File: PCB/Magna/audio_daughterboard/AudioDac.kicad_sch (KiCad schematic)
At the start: 66 parts, among them U401 PCM1789, U402 NE5532, U403 NE5532

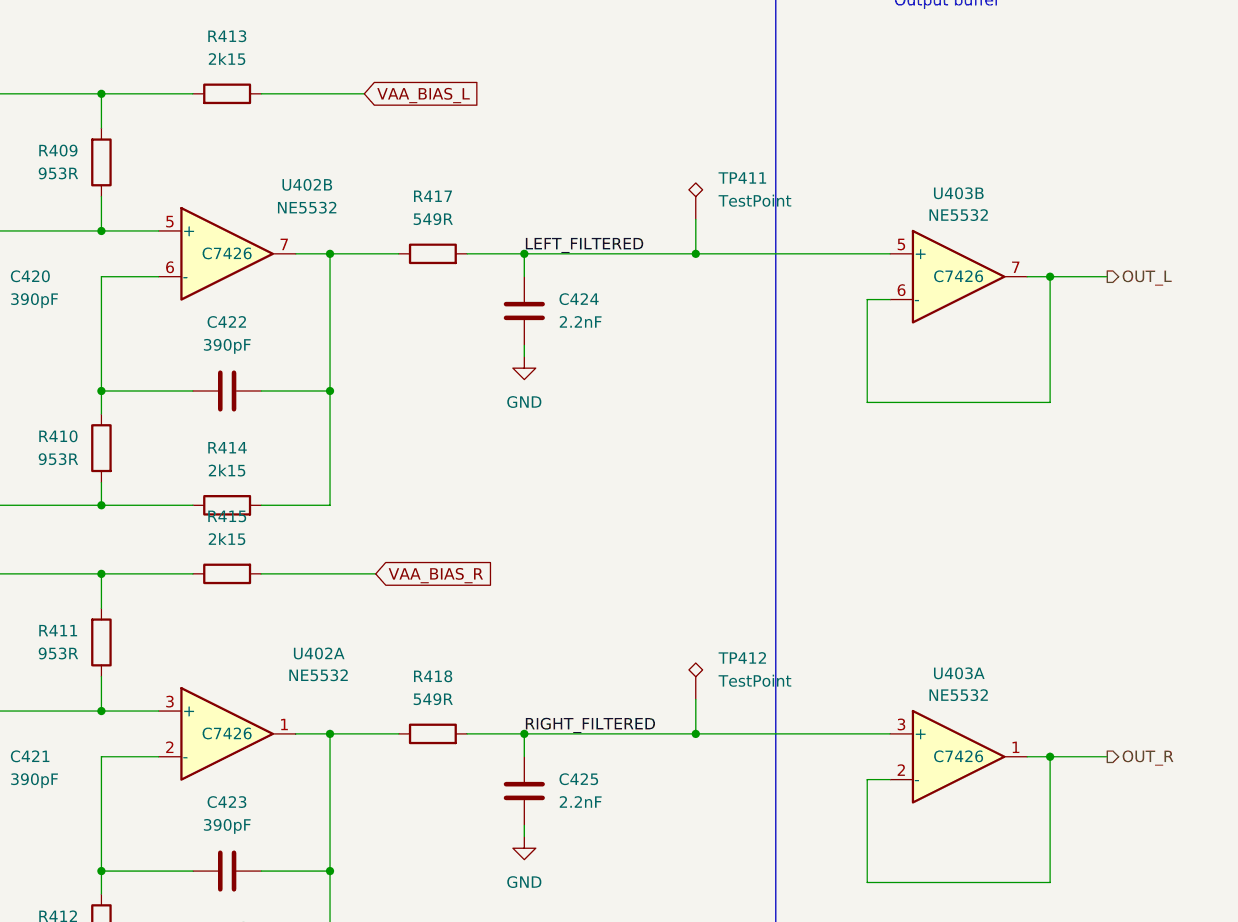
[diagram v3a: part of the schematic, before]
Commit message: Start layout and routing of Audio Daugherboard
Also a lot of small changes to everything that became apperant
when the audio daughterboard was designed. Such as the Headphone
PCB, which is now separate from the rest of the audio.
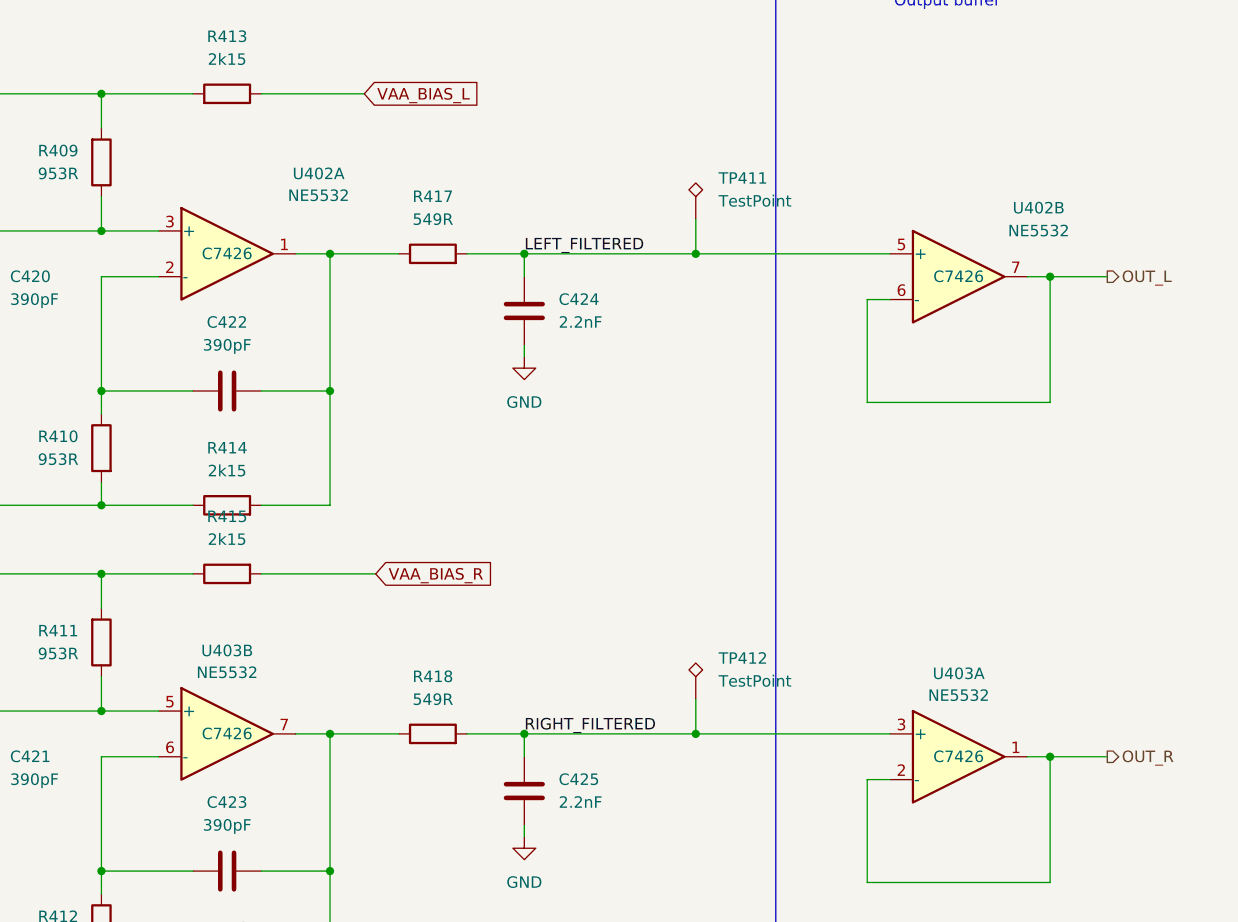
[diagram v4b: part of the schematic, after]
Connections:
- net LEFT_FILTERED: now also U402.5 (+); no longer U403.5 (+)
- net OUT_L: now also U402.6 (-), U402.7; no longer U403.6 (-), U403.7
- net at C423.1, R412.1: now also U403.6 (-); no longer U402.2 (-)
- net at C423.2, R416.2, R418.1: now also U403.7; no longer U402.1
- net at C421.1, R411.1: now also U403.5 (+); no longer U402.3 (+)
- net at C420.1, R409.1: now also U402.3 (+); no longer U402.5 (+)
- net at C422.2, R414.2, R417.1: now also U402.1; no longer U402.7
- net at C422.1, R410.1: now also U402.2 (-); no longer U402.6 (-)
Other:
- moved on the sheet: U402A, U402B, U403B
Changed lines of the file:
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@@
 	(symbol
 		(lib_id "Amplifier_Operational:NE5532")
-		(at 289.56 100.33 0)
+		(at 289.56 46.99 0)
 		(unit 1)
 		(exclude_from_sim no)
@@
 		(dnp no)
 		(property "Reference" "U402"
-			(at 299.72 91.44 0)
+			(at 299.72 38.1 0)
 			(effects
 				(font
@@
 		)
 		(property "Value" "NE5532"
-			(at 299.72 93.8643 0)
+			(at 299.72 40.5243 0)
 			(effects
 				(font
@@
 		)
 		(property "Footprint" "Package_SO:SOIC-8_3.9x4.9mm_P1.27mm"
-			(at 289.56 100.33 0)
+			(at 289.56 46.99 0)
 			(effects
 				(font
@@
 		)
 		(property "Datasheet" "http://www.ti.com/lit/ds/symlink/ne5532.pdf"
-			(at 289.56 100.33 0)
+			(at 289.56 46.99 0)
 			(effects
 				(font
@@
 		)
 		(property "Description" "Dual Low-Noise Operational Amplifiers, DIP-8/SOIC-8"
-			(at 289.56 100.33 0)
+			(at 289.56 46.99 0)
 			(effects
 				(font
@@
 		)
 		(property "Sim.Device" "SUBCKT"
-			(at 289.56 100.33 0)
+			(at 289.56 46.99 0)
 			(effects
 				(font
@@
 		)
 		(property "Sim.Library" "${KICAD7_SYMBOL_DIR}/Simulation_SPICE.sp"
-			(at 289.56 100.33 0)
+			(at 289.56 46.99 0)
 			(effects
 				(font
@@
 		)
 		(property "Sim.Name" "kicad_builtin_opamp_dual"
-			(at 289.56 100.33 0)
+			(at 289.56 46.99 0)
 			(effects
 				(font
@@
 		)
 		(property "Sim.Pins" "1=out1 2=in1- 3=in1+ 4=vee 5=in2+ 6=in2- 7=out2 8=vcc"
-			(at 289.56 100.33 0)
+			(at 289.56 46.99 0)
 			(effects
 				(font
@@
 		)
 		(property "Sim.Params" "GAIN=10M ROUT=0.3"
-			(at 289.56 100.33 0)
+			(at 289.56 46.99 0)
 			(effects
 				(font
@@
 		)
 		(property "LCSC" "C7426"
-			(at 289.56 100.33 0)
+			(at 289.56 46.99 0)
 			(effects
 				(font
@@
 		)
 		(property "Field5" ""
-			(at 289.56 100.33 0)
+			(at 289.56 46.99 0)
 			(effects
 				(font
@@
 	(symbol
 		(lib_id "Amplifier_Operational:NE5532")
-		(at 289.56 46.99 0)
+		(at 370.84 49.53 0)
 		(unit 2)
 		(exclude_from_sim no)
@@
 		(fields_autoplaced yes)
 		(property "Reference" "U402"
-			(at 298.45 39.37 0)
+			(at 379.73 41.91 0)
 			(effects
 				(font
@@
 		)
 		(property "Value" "NE5532"
-			(at 298.45 41.91 0)
+			(at 379.73 44.45 0)
 			(effects
 				(font
@@
 		)
 		(property "Footprint" "Package_SO:SOIC-8_3.9x4.9mm_P1.27mm"
-			(at 289.56 46.99 0)
+			(at 370.84 49.53 0)
 			(effects
 				(font
@@
 		)
 		(property "Datasheet" "http://www.ti.com/lit/ds/symlink/ne5532.pdf"
-			(at 289.56 46.99 0)
+			(at 370.84 49.53 0)
 			(effects
 				(font
@@
 		)
 		(property "Description" "Dual Low-Noise Operational Amplifiers, DIP-8/SOIC-8"
-			(at 289.56 46.99 0)
+			(at 370.84 49.53 0)
 			(effects
 				(font
@@
 		)
 		(property "Sim.Device" "SUBCKT"
-			(at 289.56 46.99 0)
+			(at 370.84 49.53 0)
 			(effects
 				(font
@@
 		)
 		(property "Sim.Library" "${KICAD7_SYMBOL_DIR}/Simulation_SPICE.sp"
-			(at 289.56 46.99 0)
+			(at 370.84 49.53 0)
 			(effects
 				(font
@@
 		)
 		(property "Sim.Name" "kicad_builtin_opamp_dual"
-			(at 289.56 46.99 0)
+			(at 370.84 49.53 0)
 			(effects
 				(font
@@
 		)
 		(property "Sim.Pins" "1=out1 2=in1- 3=in1+ 4=vee 5=in2+ 6=in2- 7=out2 8=vcc"
-			(at 289.56 46.99 0)
+			(at 370.84 49.53 0)
 			(effects
 				(font
@@
 		)
 		(property "Sim.Params" "GAIN=10M ROUT=0.3"
-			(at 289.56 46.99 0)
+			(at 370.84 49.53 0)
 			(effects
 				(font
@@
 		)
 		(property "LCSC" "C7426"
-			(at 289.56 46.99 0)
+			(at 370.84 49.53 0)
 			(effects
 				(font
@@
 		)
 		(property "Field5" ""
-			(at 289.56 46.99 0)
+			(at 370.84 49.53 0)
 			(effects
 				(font
@@
 	(symbol
 		(lib_id "Amplifier_Operational:NE5532")
-		(at 370.84 49.53 0)
+		(at 289.56 100.33 0)
 		(unit 2)
 		(exclude_from_sim no)
@@
 		(fields_autoplaced yes)
 		(property "Reference" "U403"
-			(at 370.84 40.3055 0)
+			(at 289.56 91.1055 0)
 			(effects
 				(font
@@
 		)
 		(property "Value" "NE5532"
-			(at 370.84 42.7298 0)
+			(at 289.56 93.5298 0)
 			(effects
 				(font
@@
 		)
 		(property "Footprint" "Package_SO:SOIC-8_3.9x4.9mm_P1.27mm"
-			(at 370.84 49.53 0)
+			(at 289.56 100.33 0)
 			(effects
 				(font
@@
 		)
 		(property "Datasheet" "http://www.ti.com/lit/ds/symlink/ne5532.pdf"
-			(at 370.84 49.53 0)
+			(at 289.56 100.33 0)
 			(effects
 				(font
@@
 		)
 		(property "Description" "Dual Low-Noise Operational Amplifiers, DIP-8/SOIC-8"
-			(at 370.84 49.53 0)
+			(at 289.56 100.33 0)
 			(effects
 				(font
@@
 		)
 		(property "Sim.Device" "SUBCKT"
-			(at 370.84 49.53 0)
+			(at 289.56 100.33 0)
 			(effects
 				(font
@@
 		)
 		(property "Sim.Library" "${KICAD7_SYMBOL_DIR}/Simulation_SPICE.sp"
-			(at 370.84 49.53 0)
+			(at 289.56 100.33 0)
 			(effects
 				(font
@@
 		)
 		(property "Sim.Name" "kicad_builtin_opamp_dual"
-			(at 370.84 49.53 0)
+			(at 289.56 100.33 0)
 			(effects
 				(font
@@
 		)
 		(property "Sim.Pins" "1=out1 2=in1- 3=in1+ 4=vee 5=in2+ 6=in2- 7=out2 8=vcc"
-			(at 370.84 49.53 0)
+			(at 289.56 100.33 0)
 			(effects
 				(font
@@
 		)
 		(property "Sim.Params" "GAIN=10M"
-			(at 370.84 49.53 0)
+			(at 289.56 100.33 0)
 			(effects
 				(font
@@
 		)
 		(property "LCSC" "C7426"
-			(at 370.84 49.53 0)
+			(at 289.56 100.33 0)
 			(effects
 				(font
@@
 		)
 		(property "Field5" ""
-			(at 370.84 49.53 0)
+			(at 289.56 100.33 0)
 			(effects
 				(font

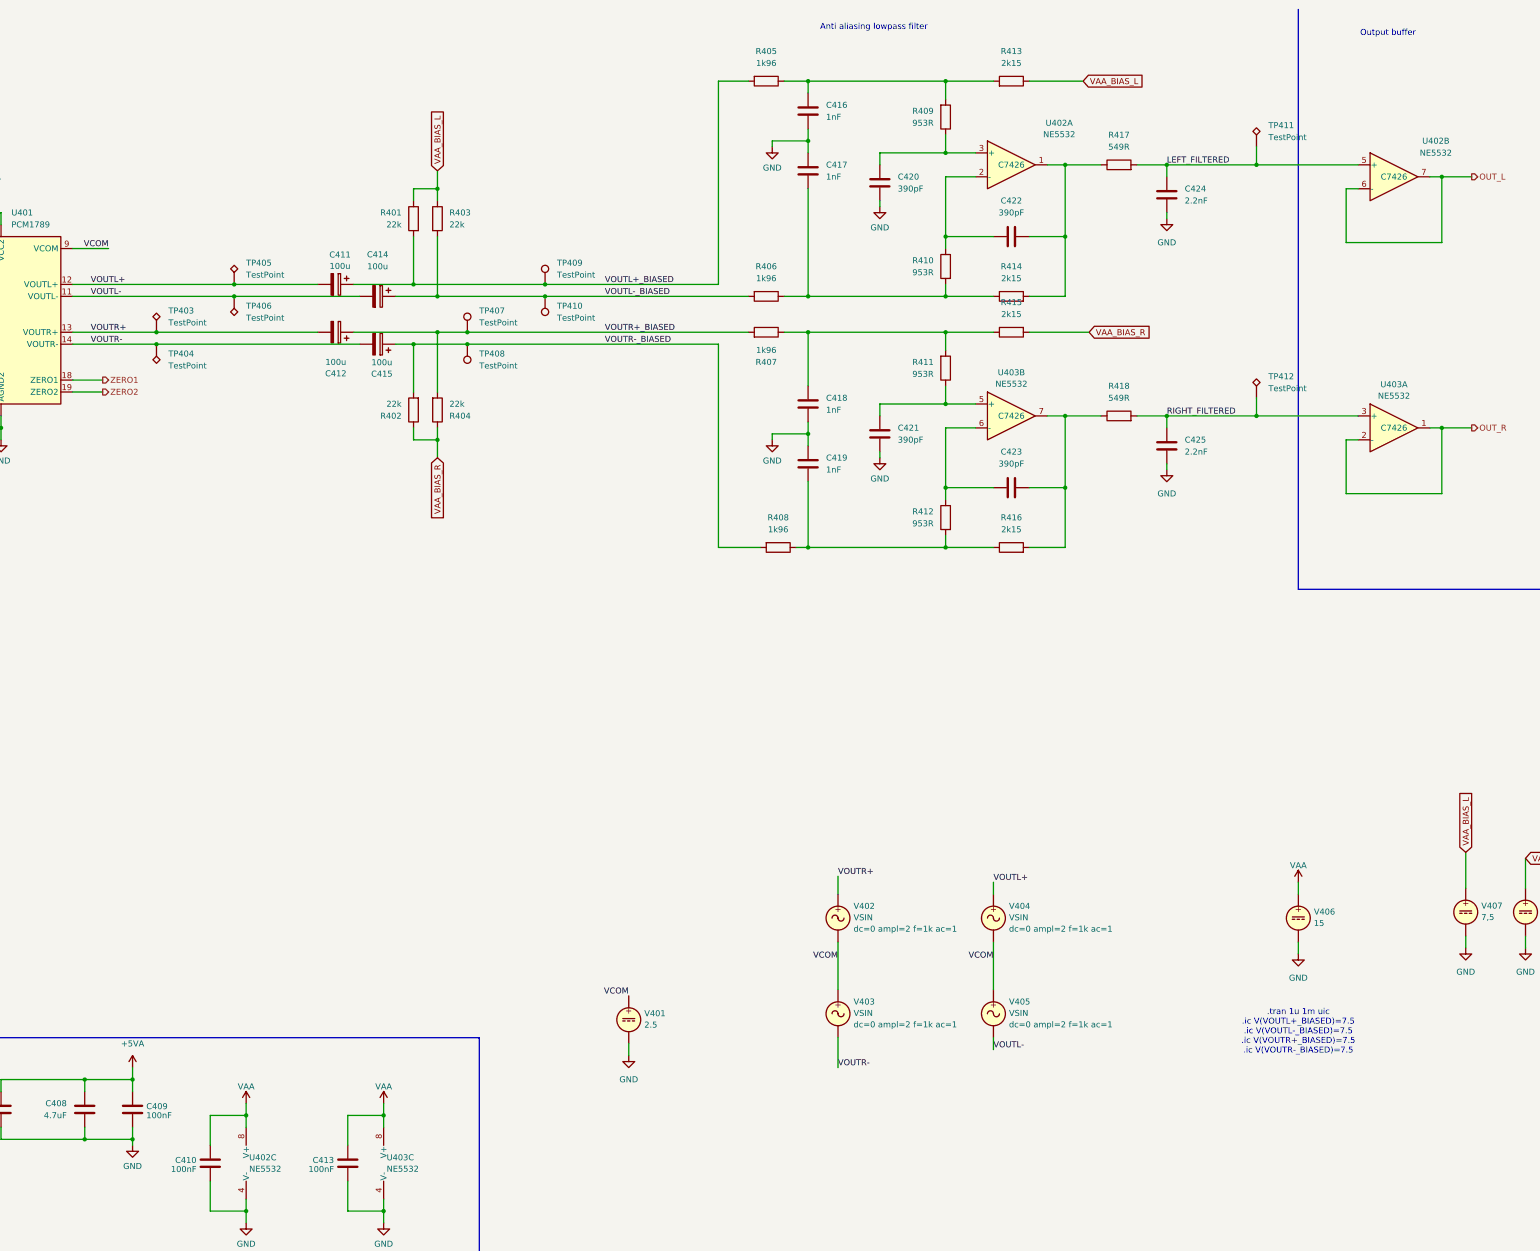
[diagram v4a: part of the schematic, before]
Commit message: Finished first round of routing for the Audio Daughterboard
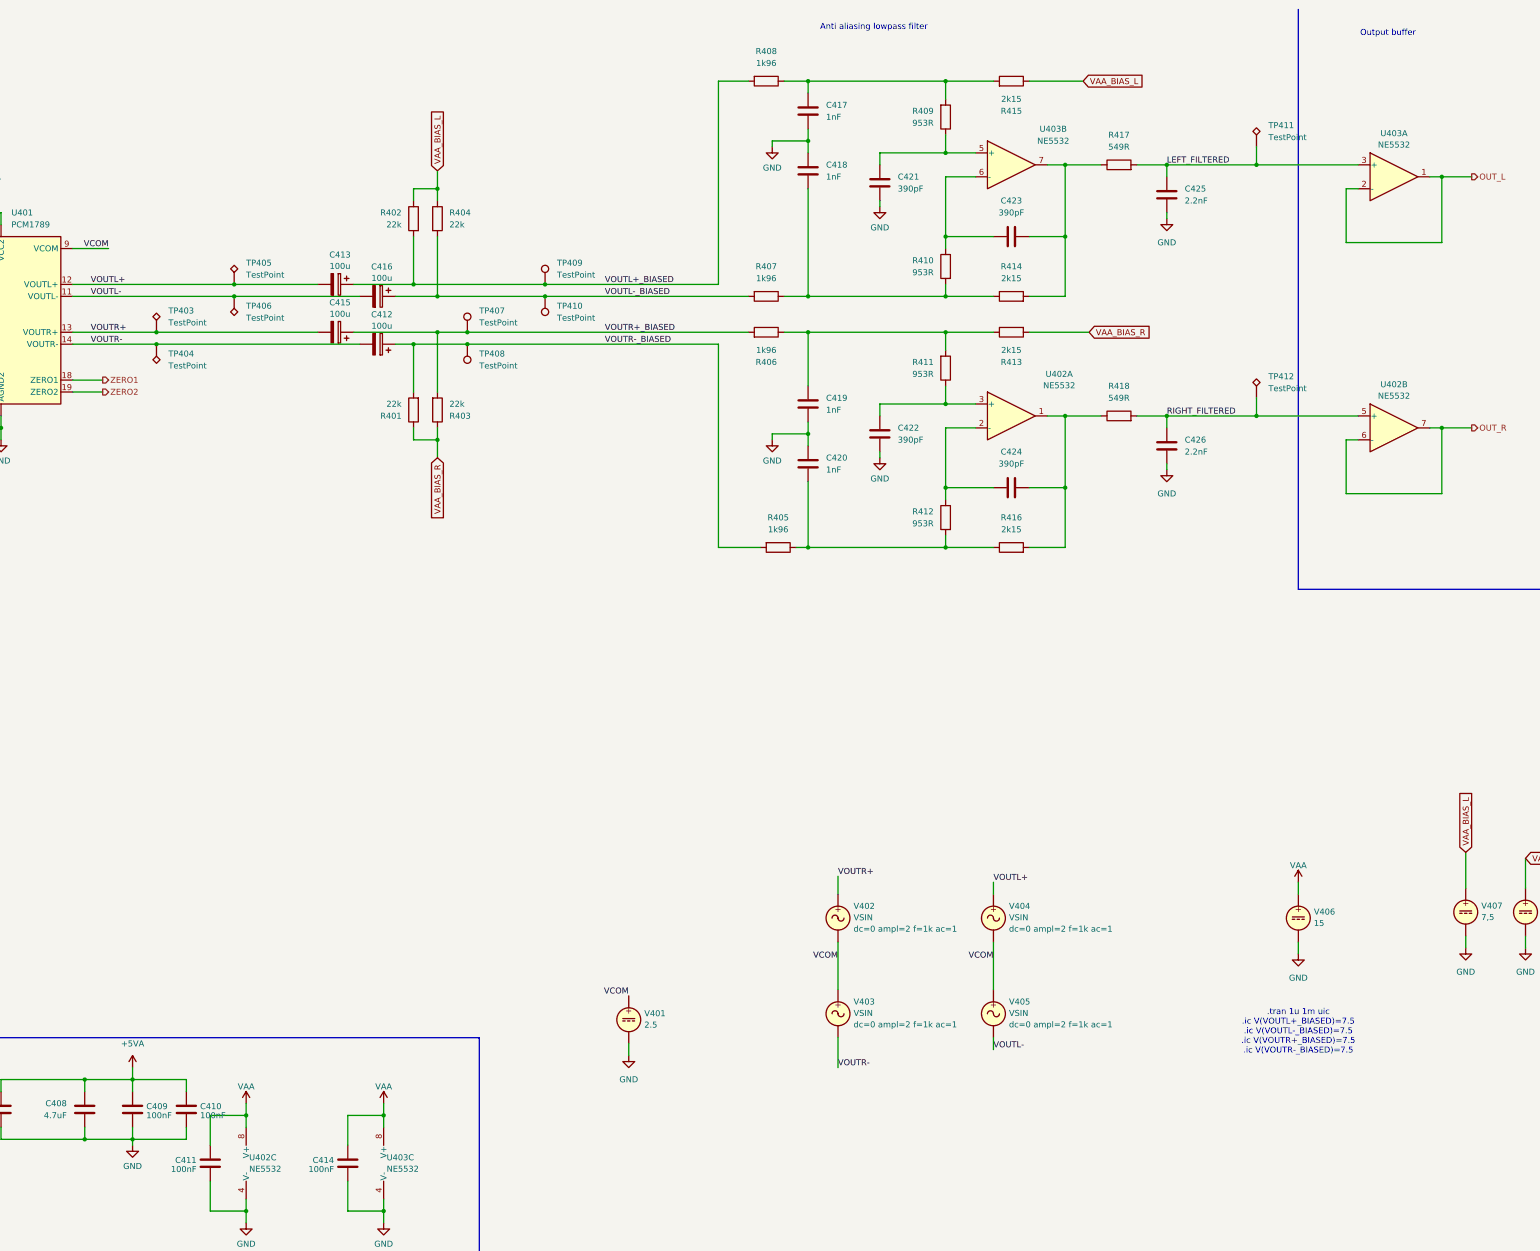
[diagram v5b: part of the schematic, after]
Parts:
- added C410: 100nF, Capacitor_SMD:C_0603_1608Metric, symbol Device:C
- R401, R402, R403, R404, R405, R406, R407, R408, R409, R410, R411, R412, R413, R414, R415, R416, R417, R418: now in the parts list
- renumbered C410 to C411, C411 to C412, C412 to C413, C413 to C414, C414 to C415, C415 to C416, C416 to C417, C417 to C418, C418 to C419, C419 to C420, C420 to C421, C421 to C422, C422 to C423, C423 to C424, C424 to C425, C425 to C426, U403 to U402, U402 to U403
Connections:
- net +5VA: now also C410.1
- net GND: now also C410.2
- net LEFT_FILTERED: now also U403.3 (+); no longer U403.5 (+)
- net OUT_L: now also U403.1, U403.2 (-); no longer U403.6 (-), U403.7
- net OUT_R: now also U402.6 (-), U402.7; no longer U403.1, U403.2 (-)
- net RIGHT_FILTERED: now also U402.5 (+); no longer U403.3 (+)
- net VAA_BIAS_L: now also R402.1, R404.1, R415.1; no longer R401.1, R403.1, R413.1
- net VAA_BIAS_R: now also R401.1, R403.1, R413.2; no longer R402.1, R404.1, R415.2
- net VOUTL+: now also C413.2; no longer C412.2
- net VOUTL+_BIASED: now also C413.1, R402.2, R408.2; no longer C412.1, R401.2, R405.2
- net VOUTL-: now also C416.2; no longer C415.2
- net VOUTL-_BIASED: now also C416.1, R404.2, R407.2; no longer C415.1, R403.2, R406.2
- net VOUTR+: now also C415.2; no longer C413.2
- net VOUTR+_BIASED: now also C415.1, R403.2, R406.2; no longer C413.1, R404.2, R407.2
- net VOUTR-: now also C412.2; no longer C416.2
- net VOUTR-_BIASED: now also C412.1, R401.2, R405.2; no longer C416.1, R402.2, R408.2
- net at C424.1, R412.1: now also U402.2 (-); no longer U402.6 (-)
- net at C424.2, R416.2, R418.1: now also U402.1; no longer U402.7
- net at C423.2, R414.2, R417.1: now also U403.7; no longer U402.1
- net at C423.1, R410.1: now also U403.6 (-); no longer U402.2 (-)
- net at C421.1, R409.1: now also U403.5 (+); no longer U402.3 (+)
- net at C422.1, R411.1: now also U402.3 (+); no longer U402.5 (+)
- net at C417.1, R409.2: now also R408.1, R415.2; no longer R405.1, R413.2
- net at C420.2, R412.2, R416.1: now also R405.1; no longer R408.1
- net at C419.1, R411.2: now also R406.1, R413.1; no longer R407.1, R415.1
- net at C418.2, R410.2, R414.1: now also R407.1; no longer R406.1
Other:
- moved on the sheet: C412, C413, C415, C416, R401, R402, R403, R404, R405, R406, R407, R408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
